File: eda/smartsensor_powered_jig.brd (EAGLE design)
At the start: 47 x 26.7 mm, 12 parts, among them J2 AVR_SPI_PRG_6PTH

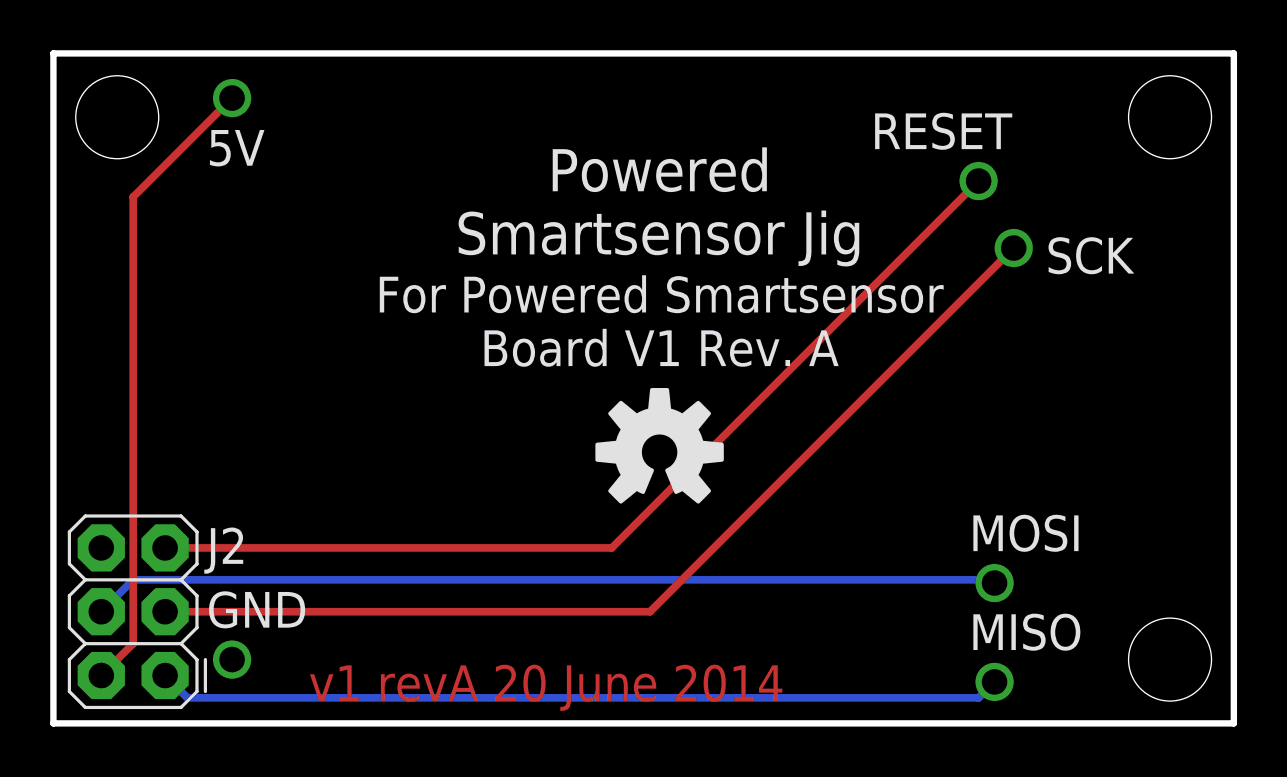
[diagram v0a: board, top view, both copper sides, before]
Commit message: Replaced 2x4 connectors with 2x5's.
On smartsensor, smartsensorPowered, smartsensor_powered_jig, and team_flag.
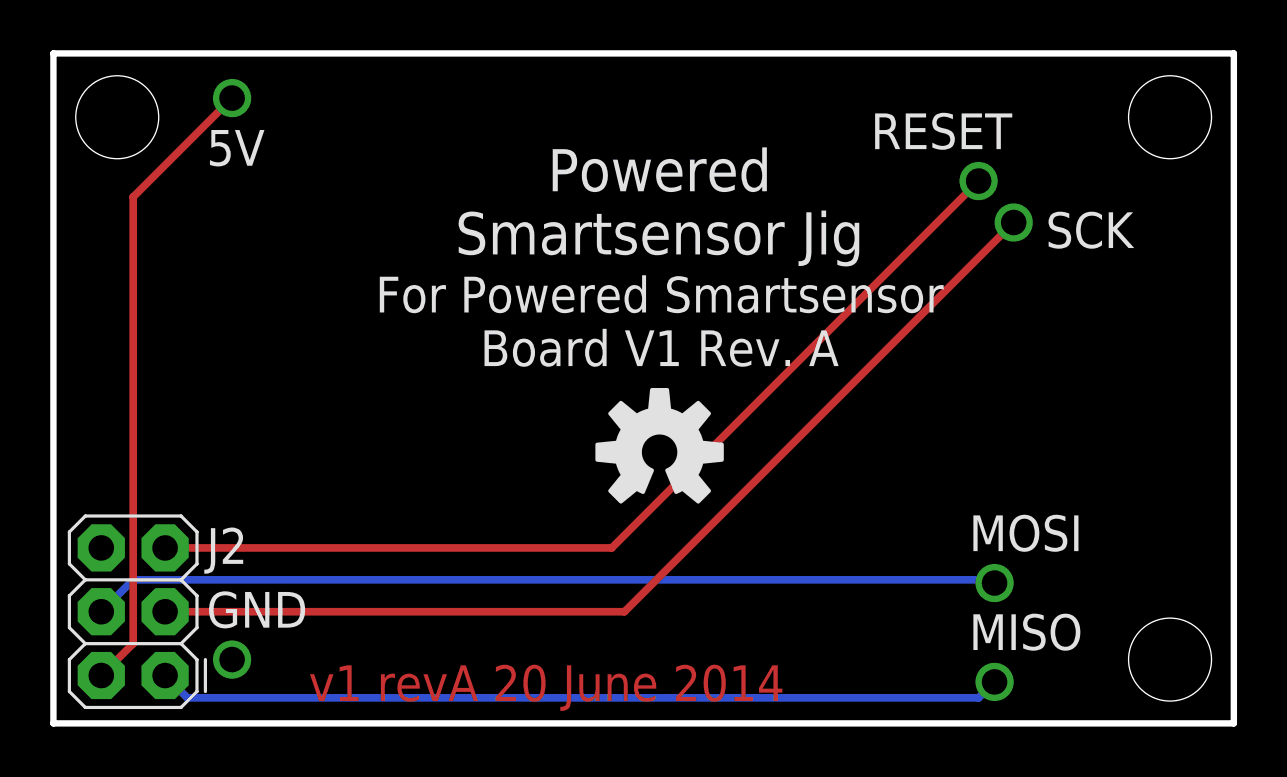
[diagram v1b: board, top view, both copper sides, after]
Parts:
- moved SCK 1.02 mm to (38.2, 19.9)
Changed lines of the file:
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@@
 <attribute name="PIE-INT-REF-NUM" value="POGO-PIN" x="37.465" y="1.651" size="1.778" layer="27" display="off"/>
 </element>
-<element name="SCK" library="pie" package="POGO_PIN_394" value="" x="38.227" y="18.923" smashed="yes">
-<attribute name="NAME" x="39.497" y="17.907" size="1.4224" layer="25" font="vector" ratio="15"/>
-<attribute name="VALUE" x="36.957" y="16.383" size="1.27" layer="27" font="vector"/>
-<attribute name="PIE-INT-REF-NUM" value="POGO-PIN" x="38.227" y="18.923" size="1.778" layer="27" display="off"/>
+<element name="SCK" library="pie" package="POGO_PIN_394" value="" x="38.227" y="19.939" smashed="yes">
+<attribute name="NAME" x="39.497" y="18.923" size="1.4224" layer="25" font="vector" ratio="15"/>
+<attribute name="VALUE" x="36.957" y="17.399" size="1.27" layer="27" font="vector"/>
+<attribute name="PIE-INT-REF-NUM" value="POGO-PIN" x="38.227" y="19.939" size="1.778" layer="27" display="off"/>
 </element>
 <element name="RESET" library="pie" package="POGO_PIN_394" value="" x="36.83" y="21.59" smashed="yes" rot="R270">
@@
 <contactref element="J2" pad="3"/>
 <contactref element="SCK" pad="POGO_PIN"/>
-<wire x1="4.445" y1="4.445" x2="23.749" y2="4.445" width="0.3048" layer="1"/>
-<wire x1="23.749" y1="4.445" x2="38.227" y2="18.923" width="0.3048" layer="1"/>
+<wire x1="4.445" y1="4.445" x2="22.733" y2="4.445" width="0.3048" layer="1"/>
+<wire x1="22.733" y1="4.445" x2="38.227" y2="19.939" width="0.3048" layer="1"/>
 </signal>
 <signal name="MISO">
@@
 </signal>
 </signals>
+<errors>
+</errors>
 </board>
 </drawing>
